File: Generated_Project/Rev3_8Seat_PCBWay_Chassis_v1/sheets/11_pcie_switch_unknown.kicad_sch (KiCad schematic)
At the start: 0 parts

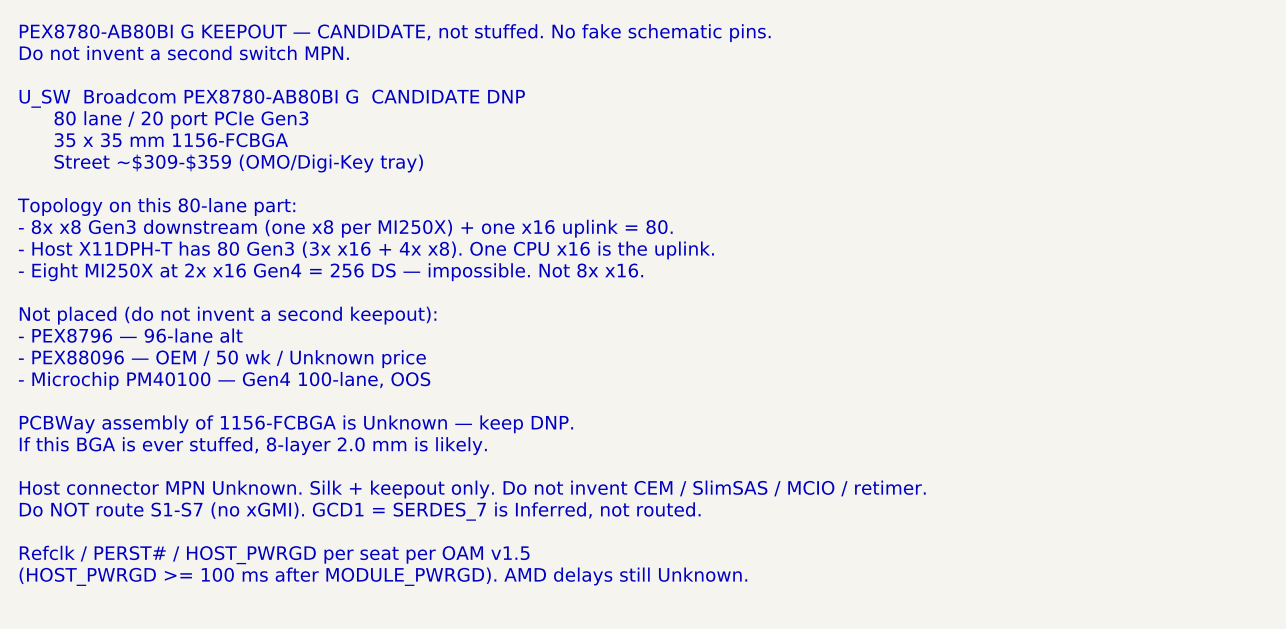
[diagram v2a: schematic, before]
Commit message: Make PM8536B-FEI the PRIMARY switch keepout (DNP x2).
Two 37.5 mm 1311-FCBGA courtyards, x8 per GCD (SW0 seats 0-3, SW1 4-7),
two CPU x16 uplinks. PEX8780 stays a cheaper 80-lane alt in docs only.
GCD1 = SERDES_7 remains Inferred. No CEM, no xGMI, do not fabricate.

Co-authored-by: zivzancoeli-commits <zivzancoeli-commits@users.noreply.github.com>
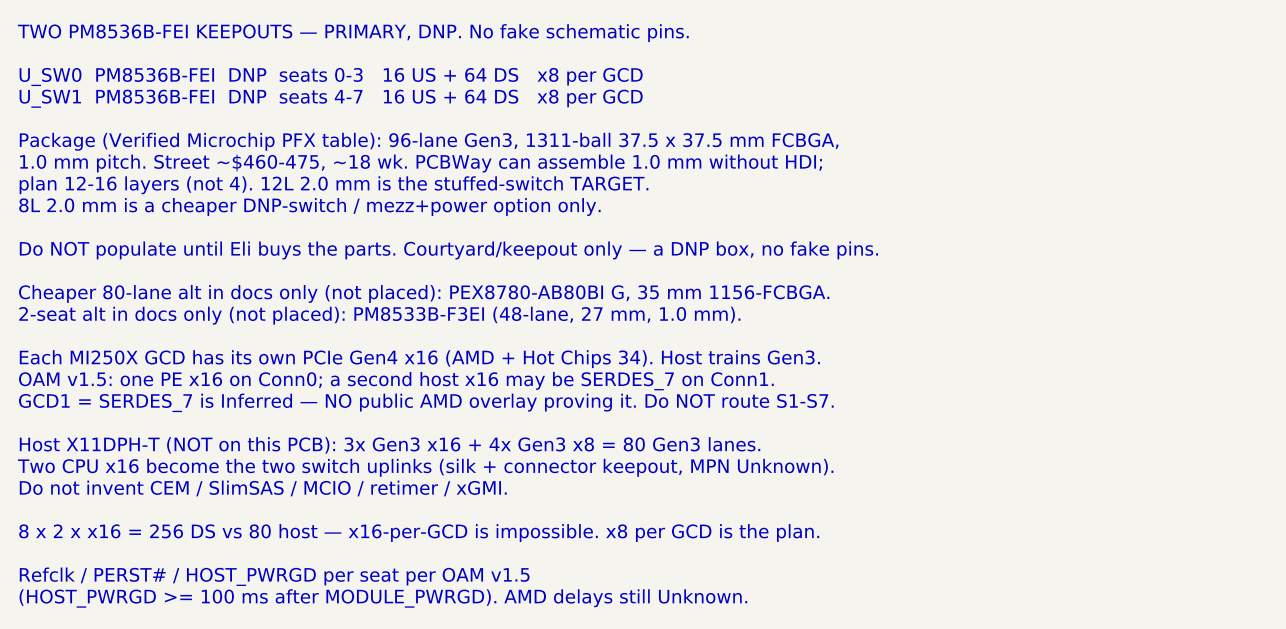
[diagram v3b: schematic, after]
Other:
- note added: "TWO PM8536B-FEI KEEPOUTS — PRIMARY, DNP. No fake schematic pins. U_SW0 PM8536B-FEI DNP seats 0-3 16 US + 64 DS x8 per GCD U_SW1 PM8536B-FEI DNP seats 4-7 16 US + 64 DS x8 per GCD Package (Verified Microchip PFX table): 96-lane Gen3, 1311-ball 37.5 x 37.5 mm FCBGA, 1.0 mm pitch. Street ~$460-475, ~18 wk. PCBWay can assemble 1.0 mm without HDI; plan 12-16 layers (not 4). 12L 2.0 mm is the stuffed-s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"
- note removed: "PEX8780-AB80BI G KEEPOUT — CANDIDATE, not stuffed. No fake schematic pins. Do not invent a second switch MPN. U_SW Broadcom PEX8780-AB80BI G CANDIDATE DNP 80 lane / 20 port PCIe Gen3 35 x 35 mm 1156-FCBGA Street ~$309-$359 (OMO/Digi-Key tray) Topology on this 80-lane part: - 8x x8 Gen3 downstream (one x8 per MI250X) + one x16 uplink = 80. - Host X11DPH-T has 80 Gen3 (3x x16 + 4x x8). One CPU x16 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"
- title: PEX8780-AB80BI G CANDIDATE (keepout, not stuffed) -> PM8536B-FEI DNP x2 PRIMARY (keepout only)
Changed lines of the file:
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@@
 	(paper "A3")
 	(title_block
-		(title "PEX8780-AB80BI G CANDIDATE (keepout, not stuffed)")
+		(title "PM8536B-FEI DNP x2 PRIMARY (keepout only)")
 		(date "2026-08-21")
 		(rev "Rev3_8Seat_PCBWay_v1")
@@
         (comment 2 "Documentation sheet — no invented nets")
         (comment 3 "Pin names: OAM Pin map rev 1.0.xlsx — OCP generic, NOT AMD overlay")
-        (comment 4 "r2.0 UNUSABLE. P3V3=Conn0 C1/C2. 12L 2.0mm stuffed-switch TARGET. Star-fed P48V.")
+        (comment 4 "r2.0 UNUSABLE. P3V3=Conn0 C1/C2. 12L 2.0mm stuffed-switch TARGET. 2x PM8536 DNP. Star-fed P48V.")
 	)
-	(text "PEX8780-AB80BI G KEEPOUT — CANDIDATE, not stuffed. No fake schematic pins.\nDo not invent a second switch MPN.\n\nU_SW  Broadcom PEX8780-AB80BI G  CANDIDATE DNP\n      80 lane / 20 port PCIe Gen3\n      35 x 35 mm 1156-FCBGA\n      Street ~$309-$359 (OMO/Digi-Key tray)\n\nTopology on this 80-lane part:\n- 8x x8 Gen3 downstream (one x8 per MI250X) + one x16 uplink = 80.\n- Host X11DPH-T has 80 Gen3 (3x x16 + 4x x8). One CPU x16 is the uplink.\n- Eight MI250X at 2x x16 Gen4 = 256 DS — impossible. Not 8x x16.\n\nNot placed (do not invent a second keepout):\n- PEX8796 — 96-lane alt\n- PEX88096 — OEM / 50 wk / Unknown price\n- Microchip PM40100 — Gen4 100-lane, OOS\n\nPCBWay assembly of 1156-FCBGA is Unknown — keep DNP.\nIf this BGA is ever stuffed, 8-layer 2.0 mm is likely.\n\nHost connector MPN Unknown. Silk + keepout only. Do not invent CEM / SlimSAS / MCIO / retimer.\nDo NOT route S1-S7 (no xGMI). GCD1 = SERDES_7 is Inferred, not routed.\n\nRefclk / PERST# / HOST_PWRGD per seat per OAM v1.5\n(HOST_PWRGD >= 100 ms after MODULE_PWRGD). AMD delays still Unknown.\n"
+	(text "TWO PM8536B-FEI KEEPOUTS — PRIMARY, DNP. No fake schematic pins.\n\nU_SW0  PM8536B-FEI  DNP  seats 0-3   16 US + 64 DS   x8 per GCD\nU_SW1  PM8536B-FEI  DNP  seats 4-7   16 US + 64 DS   x8 per GCD\n\nPackage (Verified Microchip PFX table): 96-lane Gen3, 1311-ball 37.5 x 37.5 mm FCBGA,\n1.0 mm pitch. Street ~$460-475, ~18 wk. PCBWay can assemble 1.0 mm without HDI;\nplan 12-16 layers (not 4). 12L 2.0 mm is the stuffed-switch TARGET.\n8L 2.0 mm is a cheaper DNP-switch / mezz+power option only.\n\nDo NOT populate until Eli buys the parts. Courtyard/keepout only — a DNP box, no fake pins.\n\nCheaper 80-lane alt in docs only (not placed): PEX8780-AB80BI G, 35 mm 1156-FCBGA.\n2-seat alt in docs only (not placed): PM8533B-F3EI (48-lane, 27 mm, 1.0 mm).\n\nEach MI250X GCD has its own PCIe Gen4 x16 (AMD + Hot Chips 34). Host trains Gen3.\nOAM v1.5: one PE x16 on Conn0; a second host x16 may be SERDES_7 on Conn1.\nGCD1 = SERDES_7 is Inferred — NO public AMD overlay proving it. Do NOT route S1-S7.\n\nHost X11DPH-T (NOT on this PCB): 3x Gen3 x16 + 4x Gen3 x8 = 80 Gen3 lanes.\nTwo CPU x16 become the two switch uplinks (silk + connector keepout, MPN Unknown).\nDo not invent CEM / SlimSAS / MCIO / retimer / xGMI.\n\n8 x 2 x x16 = 256 DS vs 80 host — x16-per-GCD is impossible. x8 per GCD is the plan.\n\nRefclk / PERST# / HOST_PWRGD per seat per OAM v1.5\n(HOST_PWRGD >= 100 ms after MODULE_PWRGD). AMD delays still Unknown.\n"
 		(exclude_from_sim no)
 		(at 20.32 20.32 0)

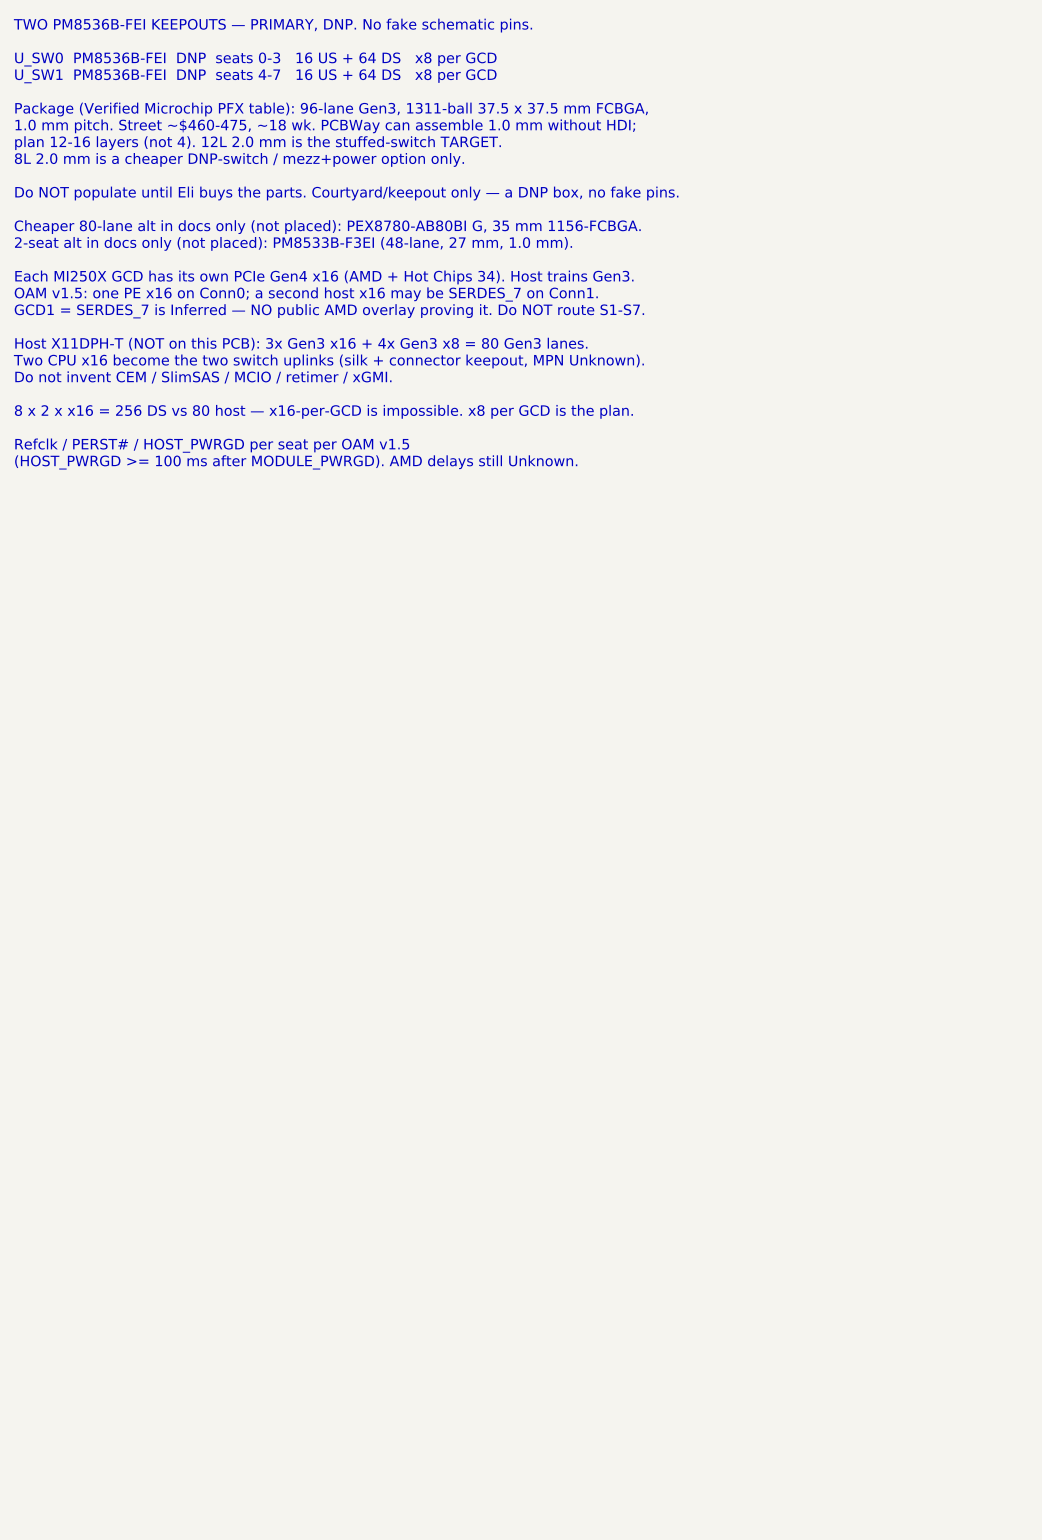
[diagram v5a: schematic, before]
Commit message: Make the Rev3 8-seat chassis full-width capable with four PM8536 DNP courtyards.
Same 492x372 POWER+MECH PCB; architecture is now 16 named x16 PE buses
(PE_Sn_GCD0_x16 + PE_Sn_GCD1_x16) and SW0-SW3 keepouts. Two 96-lane
switches are enough for 8x x8/GCD, not 8x x16/GCD. Host stays X11DPH-T
(~80 lanes) and cannot light 256 downstream. Do not energize P48V.

Co-authored-by: zivzancoeli-commits <zivzancoeli-commits@users.noreply.github.com>
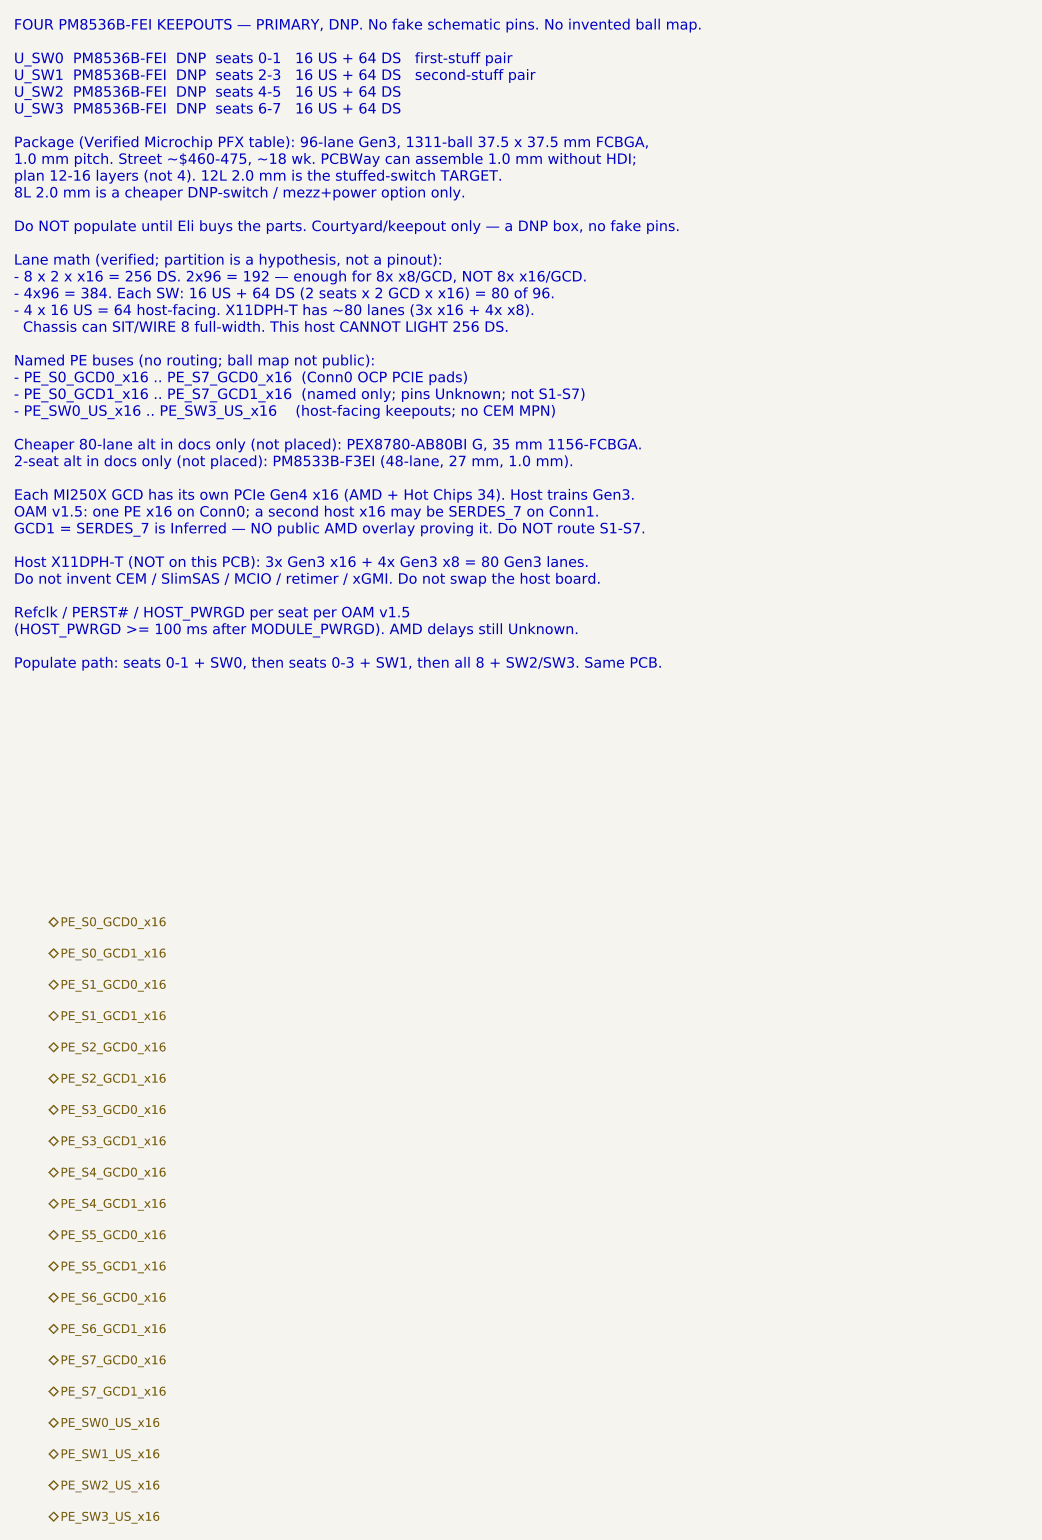
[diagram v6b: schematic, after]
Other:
- note added: "FOUR PM8536B-FEI KEEPOUTS — PRIMARY, DNP. No fake schematic pins. No invented ball map. U_SW0 PM8536B-FEI DNP seats 0-1 16 US + 64 DS first-stuff pair U_SW1 PM8536B-FEI DNP seats 2-3 16 US + 64 DS second-stuff pair U_SW2 PM8536B-FEI DNP seats 4-5 16 US + 64 DS U_SW3 PM8536B-FEI DNP seats 6-7 16 US + 64 DS Package (Verified Microchip PFX table): 96-lane Gen3, 1311-ball 37.5 x 37.5 mm FCBGA, 1.0 mm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"
- note removed: "TWO PM8536B-FEI KEEPOUTS — PRIMARY, DNP. No fake schematic pins. U_SW0 PM8536B-FEI DNP seats 0-3 16 US + 64 DS x8 per GCD U_SW1 PM8536B-FEI DNP seats 4-7 16 US + 64 DS x8 per GCD Package (Verified Microchip PFX table): 96-lane Gen3, 1311-ball 37.5 x 37.5 mm FCBGA, 1.0 mm pitch. Street ~$460-475, ~18 wk. PCBWay can assemble 1.0 mm without HDI; plan 12-16 layers (not 4). 12L 2.0 mm is the stuffed-s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"
- title: PM8536B-FEI DNP x2 PRIMARY (keepout only) -> PM8536B-FEI DNP x4 PRIMARY (keepout only)
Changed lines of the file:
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@@
 	(paper "A3")
 	(title_block
-		(title "PM8536B-FEI DNP x2 PRIMARY (keepout only)")
+		(title "PM8536B-FEI DNP x4 PRIMARY (keepout only)")
 		(date "2026-08-22")
 		(rev "Rev3_8Seat_PCBWay_v1")
@@
         (comment 2 "Documentation sheet — no invented nets")
         (comment 3 "Pin names: OAM Pin map rev 1.0.xlsx — OCP generic, NOT AMD overlay")
-        (comment 4 "r2.0 UNUSABLE. P3V3=Conn0 C1/C2. 12L 2.0mm stuffed-switch TARGET. 2x PM8536 DNP. Star-fed P48V.")
+        (comment 4 "r2.0 UNUSABLE. P3V3=Conn0 C1/C2. 12L 2.0mm stuffed-switch TARGET. 4x PM8536 DNP. Star-fed P48V.")
 	)
-	(text "TWO PM8536B-FEI KEEPOUTS — PRIMARY, DNP. No fake schematic pins.\n\nU_SW0  PM8536B-FEI  DNP  seats 0-3   16 US + 64 DS   x8 per GCD\nU_SW1  PM8536B-FEI  DNP  seats 4-7   16 US + 64 DS   x8 per GCD\n\nPackage (Verified Microchip PFX table): 96-lane Gen3, 1311-ball 37.5 x 37.5 mm FCBGA,\n1.0 mm pitch. Street ~$460-475, ~18 wk. PCBWay can assemble 1.0 mm without HDI;\nplan 12-16 layers (not 4). 12L 2.0 mm is the stuffed-switch TARGET.\n8L 2.0 mm is a cheaper DNP-switch / mezz+power option only.\n\nDo NOT populate until Eli buys the parts. Courtyard/keepout only — a DNP box, no fake pins.\n\nCheaper 80-lane alt in docs only (not placed): PEX8780-AB80BI G, 35 mm 1156-FCBGA.\n2-seat alt in docs only (not placed): PM8533B-F3EI (48-lane, 27 mm, 1.0 mm).\n\nEach MI250X GCD has its own PCIe Gen4 x16 (AMD + Hot Chips 34). Host trains Gen3.\nOAM v1.5: one PE x16 on Conn0; a second host x16 may be SERDES_7 on Conn1.\nGCD1 = SERDES_7 is Inferred — NO public AMD overlay proving it. Do NOT route S1-S7.\n\nHost X11DPH-T (NOT on this PCB): 3x Gen3 x16 + 4x Gen3 x8 = 80 Gen3 lanes.\nTwo CPU x16 become the two switch uplinks (silk + connector keepout, MPN Unknown).\nDo not invent CEM / SlimSAS / MCIO / retimer / xGMI.\n\n8 x 2 x x16 = 256 DS vs 80 host — x16-per-GCD is impossible. x8 per GCD is the plan.\n\nRefclk / PERST# / HOST_PWRGD per seat per OAM v1.5\n(HOST_PWRGD >= 100 ms after MODULE_PWRGD). AMD delays still Unknown.\n"
+	(text "FOUR PM8536B-FEI KEEPOUTS — PRIMARY, DNP. No fake schematic pins. No invented ball map.\n\nU_SW0  PM8536B-FEI  DNP  seats 0-1   16 US + 64 DS   first-stuff pair\nU_SW1  PM8536B-FEI  DNP  seats 2-3   16 US + 64 DS   second-stuff pair\nU_SW2  PM8536B-FEI  DNP  seats 4-5   16 US + 64 DS\nU_SW3  PM8536B-FEI  DNP  seats 6-7   16 US + 64 DS\n\nPackage (Verified Microchip PFX table): 96-lane Gen3, 1311-ball 37.5 x 37.5 mm FCBGA,\n1.0 mm pitch. Street ~$460-475, ~18 wk. PCBWay can assemble 1.0 mm without HDI;\nplan 12-16 layers (not 4). 12L 2.0 mm is the stuffed-switch TARGET.\n8L 2.0 mm is a cheaper DNP-switch / mezz+power option only.\n\nDo NOT populate until Eli buys the parts. Courtyard/keepout only — a DNP box, no fake pins.\n\nLane math (verified; partition is a hypothesis, not a pinout):\n- 8 x 2 x x16 = 256 DS. 2x96 = 192 — enough for 8x x8/GCD, NOT 8x x16/GCD.\n- 4x96 = 384. Each SW: 16 US + 64 DS (2 seats x 2 GCD x x16) = 80 of 96.\n- 4 x 16 US = 64 host-facing. X11DPH-T has ~80 lanes (3x x16 + 4x x8).\n  Chassis can SIT/WIRE 8 full-width. This host CANNOT LIGHT 256 DS.\n\nNamed PE buses (no routing; ball map not public):\n- PE_S0_GCD0_x16 .. PE_S7_GCD0_x16  (Conn0 OCP PCIE pads)\n- PE_S0_GCD1_x16 .. PE_S7_GCD1_x16  (named only; pins Unknown; not S1-S7)\n- PE_SW0_US_x16 .. PE_SW3_US_x16    (host-facing keepouts; no CEM MPN)\n\nCheaper 80-lane alt in docs only (not placed): PEX8780-AB80BI G, 35 mm 1156-FCBGA.\n2-seat alt in docs only (not placed): PM8533B-F3EI (48-lane, 27 mm, 1.0 mm).\n\nEach MI250X GCD has its own PCIe Gen4 x16 (AMD + Hot Chips 34). Host trains Gen3.\nOAM v1.5: one PE x16 on Conn0; a second host x16 may be SERDES_7 on Conn1.\nGCD1 = SERDES_7 is Inferred — NO public AMD overlay proving it. Do NOT route S1-S7.\n\nHost X11DPH-T (NOT on this PCB): 3x Gen3 x16 + 4x Gen3 x8 = 80 Gen3 lanes.\nDo not invent CEM / SlimSAS / MCIO / retimer / xGMI. Do not swap the host board.\n\nRefclk / PERST# / HOST_PWRGD per seat per OAM v1.5\n(HOST_PWRGD >= 100 ms after MODULE_PWRGD). AMD delays still Unknown.\n\nPopulate path: seats 0-1 + SW0, then seats 0-3 + SW1, then all 8 + SW2/SW3. Same PCB.\n"
 		(exclude_from_sim no)
 		(at 20.32 20.32 0)
 		(effects (font (size 1.5 1.5)) (justify left top))
 	)
+	(hierarchical_label "PE_S0_GCD0_x16"
+		(shape bidirectional)
+		(at 25.4 150 0)
+		(effects (font (size 1.27 1.27)) (justify left))
+	)
+	(hierarchical_label "PE_S0_GCD1_x16"
+		(shape bidirectional)
+		(at 25.4 154.5 0)
+		(effects (font (size 1.27 1.27)) (justify left))
+	)
+	(hierarchical_label "PE_S1_GCD0_x16"
+		(shape bidirectional)
+		(at 25.4 159.0 0)
+		(effects (font (size 1.27 1.27)) (justify left))
+	)
+	(hierarchical_label "PE_S1_GCD1_x16"
+		(shape bidirectional)
+		(at 25.4 163.5 0)
+		(effects (font (size 1.27 1.27)) (justify left))
+	)
+	(hierarchical_label "PE_S2_GCD0_x16"
+		(shape bidirectional)
+		(at 25.4 168.0 0)
+		(effects (font (size 1.27 1.27)) (justify left))
+	)
+	(hierarchical_label "PE_S2_GCD1_x16"
+		(shape bidirectional)
+		(at 25.4 172.5 0)
+		(effects (font (size 1.27 1.27)) (justify left))
+	)
+	(hierarchical_label "PE_S3_GCD0_x16"
+		(shape bidirectional)
+		(at 25.4 177.0 0)
+		(effects (font (size 1.27 1.27)) (justify left))
+	)
+	(hierarchical_label "PE_S3_GCD1_x16"
+		(shape bidirectional)
+		(at 25.4 181.5 0)
+		(effects (font (size 1.27 1.27)) (justify left))
+	)
+	(hierarchical_label "PE_S4_GCD0_x16"
+		(shape bidirectional)
+		(at 25.4 186.0 0)
+		(effects (font (size 1.27 1.27)) (justify left))
+	)
+	(hierarchical_label "PE_S4_GCD1_x16"
+		(shape bidirectional)
+		(at 25.4 190.5 0)
+		(effects (font (size 1.27 1.27)) (justify left))
+	)
+	(hierarchical_label "PE_S5_GCD0_x16"
+		(shape bidirectional)
+		(at 25.4 195.0 0)
+		(effects (font (size 1.27 1.27)) (justify left))
+	)
+	(hierarchical_label "PE_S5_GCD1_x16"
+		(shape bidirectional)
+		(at 25.4 199.5 0)
+		(effects (font (size 1.27 1.27)) (justify left))
+	)
+	(hierarchical_label "PE_S6_GCD0_x16"
+		(shape bidirectional)
+		(at 25.4 204.0 0)
+		(effects (font (size 1.27 1.27)) (justify left))
+	)
+	(hierarchical_label "PE_S6_GCD1_x16"
+		(shape bidirectional)
+		(at 25.4 208.5 0)
+		(effects (font (size 1.27 1.27)) (justify left))
+	)
+	(hierarchical_label "PE_S7_GCD0_x16"
+		(shape bidirectional)
+		(at 25.4 213.0 0)
+		(effects (font (size 1.27 1.27)) (justify left))
+	)
+	(hierarchical_label "PE_S7_GCD1_x16"
+		(shape bidirectional)
+		(at 25.4 217.5 0)
+		(effects (font (size 1.27 1.27)) (justify left))
+	)
+	(hierarchical_label "PE_SW0_US_x16"
+		(shape bidirectional)
+		(at 25.4 222.0 0)
+		(effects (font (size 1.27 1.27)) (justify left))
+	)
+	(hierarchical_label "PE_SW1_US_x16"
+		(shape bidirectional)
+		(at 25.4 226.5 0)
+		(effects (font (size 1.27 1.27)) (justify left))
+	)
+	(hierarchical_label "PE_SW2_US_x16"
+		(shape bidirectional)
+		(at 25.4 231.0 0)
+		(effects (font (size 1.27 1.27)) (justify left))
+	)
+	(hierarchical_label "PE_SW3_US_x16"
+		(shape bidirectional)
+		(at 25.4 235.5 0)
+		(effects (font (size 1.27 1.27)) (justify left))
+	)
 	(sheet_instances
